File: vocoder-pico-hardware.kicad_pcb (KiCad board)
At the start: 2 copper layers, 57 x 108 mm, 68 parts, among them J1 Conn_02x05_Odd_Even, J2 AudioJack2_SwitchT, J3 AudioJack2_SwitchT, Q1 BC547, Q2 BC547, Q3 BC547, Q4 BC547, SW1 SW_Push, SW2 SW_Push, U1 TL072, U2 LM7805_TO220, U3 PCM5100A, U4 SC39-11GWA, U5 SC39-11GWA, U6 SC39-11GWA, U7 SC39-11GWA, U8 MCP6002-xP

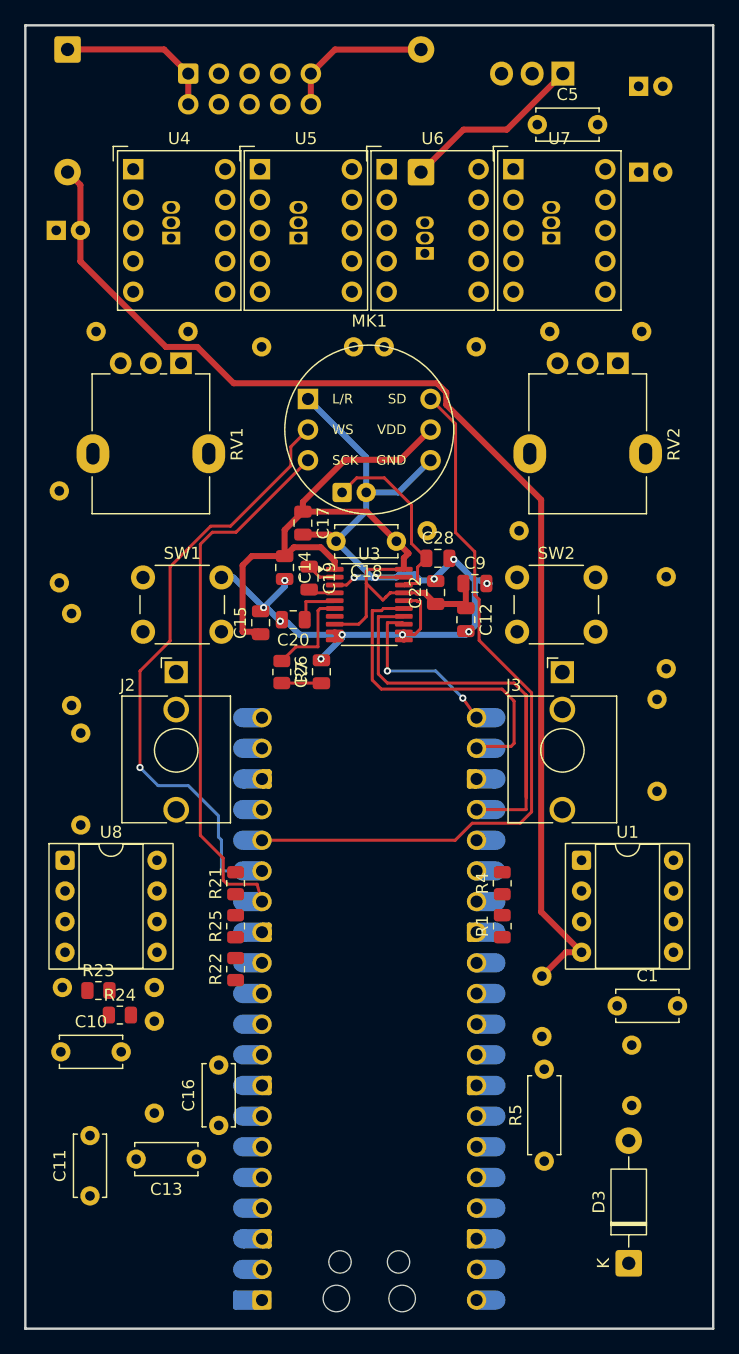
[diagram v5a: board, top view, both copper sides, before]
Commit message: improve power supply placement and routing
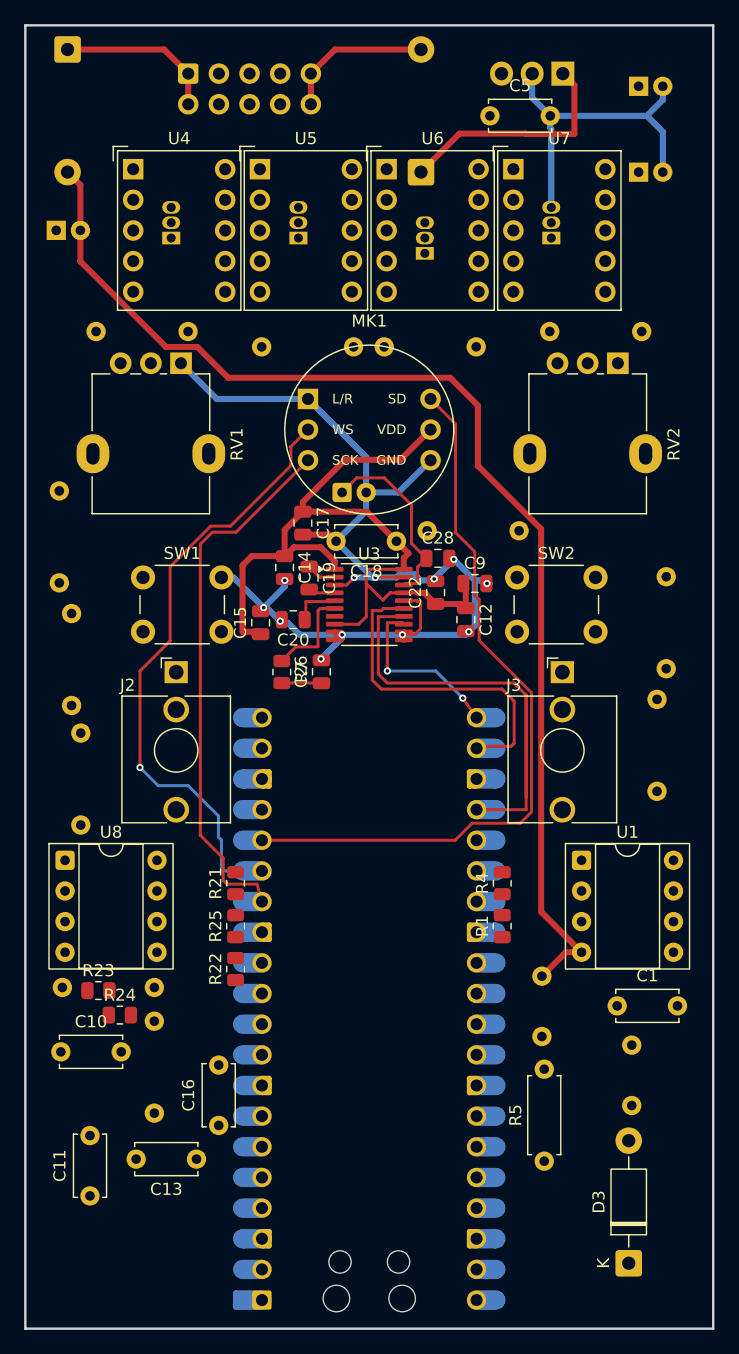
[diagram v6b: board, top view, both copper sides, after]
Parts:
- moved C5 3.99 mm to (87.5, 37.5)
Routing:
- net GND: track 86.9 -> 126.6 mm
- net +12V: track 15.1 -> 19.4 mm
- net -12V: track 97.8 -> 98.7 mm
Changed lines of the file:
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@@
 	(footprint "Capacitor_THT:C_Disc_D5.0mm_W2.5mm_P5.00mm"
 		(layer "F.Cu")
-		(at 91.4235 38.227)
+		(at 87.5 37.5)
 		(descr "C, Disc series, Radial, pin pitch=5.00mm, diameter*width=5*2.5mm^2, Capacitor, http://cdn-reichelt.de/documents/datenblatt/B300/DS_KERKO_TC.pdf")
 		(tags "C Disc series Radial pin pitch 5.00mm diameter 5mm width 2.5mm Capacitor")
@@
 	)
 	(segment
+		(start 101.822 36.18337)
+		(end 101.822 35.052)
+		(width 0.5)
+		(layer "B.Cu")
+		(net 1)
+	)
+	(segment
+		(start 72.42 60.96)
+		(end 64.86 60.96)
+		(width 0.5)
+		(layer "B.Cu")
+		(net 1)
+	)
+	(segment
 		(start 86.25 76)
 		(end 84.5 74.25)
@@
 	)
 	(segment
+		(start 100.50537 37.5)
+		(end 101.822 38.81663)
+		(width 0.5)
+		(layer "B.Cu")
+		(net 1)
+	)
+	(segment
 		(start 84.25 74)
 		(end 84.25 74.5)
@@
 	)
 	(segment
+		(start 91 36)
+		(end 91 34)
+		(width 0.5)
+		(layer "B.Cu")
+		(net 1)
+	)
+	(segment
 		(start 79.75 75.75)
 		(end 78 75.75)
@@
 	)
 	(segment
+		(start 92.5 37.5)
+		(end 91 36)
+		(width 0.5)
+		(layer "B.Cu")
+		(net 1)
+	)
+	(segment
 		(start 81.25 75.5)
 		(end 80 75.5)
@@
 	)
 	(segment
+		(start 92.583 38.583)
+		(end 92.583 45.085)
+		(width 0.5)
+		(layer "B.Cu")
+		(net 1)
+	)
+	(segment
 		(start 77.75 75.75)
 		(end 74.75 72.75)
@@
 	)
 	(segment
+		(start 92.5 37.5)
+		(end 92.5 38.5)
+		(width 0.5)
+		(layer "B.Cu")
+		(net 1)
+	)
+	(segment
 		(start 85.5 80.5)
 		(end 85.75 80.25)
@@
 	)
 	(segment
+		(start 92.5 38.5)
+		(end 92.583 38.583)
+		(width 0.5)
+		(layer "B.Cu")
+		(net 1)
+	)
+	(segment
+		(start 64.86 60.96)
+		(end 61.9 58)
+		(width 0.5)
+		(layer "B.Cu")
+		(net 1)
+	)
+	(segment
+		(start 92.5 37.5)
+		(end 100.50537 37.5)
+		(width 0.5)
+		(layer "B.Cu")
+		(net 1)
+	)
+	(segment
 		(start 80.25 80.5)
 		(end 85.5 80.5)
@@
 	)
 	(segment
+		(start 100.50537 37.5)
+		(end 101.822 36.18337)
+		(width 0.5)
+		(layer "B.Cu")
+		(net 1)
+	)
+	(segment
 		(start 84.5 74.25)
 		(end 84.25 74)
@@
 	)
 	(segment
+		(start 101.822 38.81663)
+		(end 101.822 42.164)
+		(width 0.5)
+		(layer "B.Cu")
+		(net 1)
+	)
+	(segment
 		(start 87.25 76.25)
 		(end 87.5 76.25)
@@
 	)
 	(segment
-		(start 60.649 56.649)
-		(end 63.251 56.649)
+		(start 91.744308 71.744308)
+		(end 91.744308 103.464308)
 		(width 0.5)
 		(layer "F.Cu")
@@
 	)
 	(segment
-		(start 91.744308 69.30972)
-		(end 91.744308 103.464308)
+		(start 84.199 59.199)
+		(end 86.5 61.5)
 		(width 0.5)
 		(layer "F.Cu")
@@
 	)
 	(segment
-		(start 83.881 60.421108)
-		(end 83.881 61.446412)
+		(start 91.744308 103.464308)
+		(end 95.09 106.81)
 		(width 0.5)
 		(layer "F.Cu")
@@
 	)
 	(segment
-		(start 53.562 49.562)
-		(end 60.649 56.649)
+		(start 95.09 106.81)
+		(end 93.787 106.81)
 		(width 0.5)
 		(layer "F.Cu")
@@
 	)
 	(segment
-		(start 95.09 106.81)
-		(end 93.787 106.81)
+		(start 86.5 61.5)
+		(end 86.5 66.5)
 		(width 0.5)
 		(layer "F.Cu")
@@
 	)
 	(segment
-		(start 91.744308 103.464308)
-		(end 95.09 106.81)
+		(start 65.801 59.199)
+		(end 84.199 59.199)
 		(width 0.5)
 		(layer "F.Cu")
@@
 	)
 	(segment
-		(start 53.562 43.222)
-		(end 53.562 46.99)
+		(start 63.251 56.649)
+		(end 65.801 59.199)
 		(width 0.5)
 		(layer "F.Cu")
@@
 	)
 	(segment
-		(start 53.562 46.99)
-		(end 53.562 49.562)
+		(start 53.562 43.222)
+		(end 53.562 46.99)
 		(width 0.5)
 		(layer "F.Cu")
@@
 	)
 	(segment
-		(start 66.261 59.659)
-		(end 83.118892 59.659)
+		(start 86.5 66.5)
+		(end 91.744308 71.744308)
 		(width 0.5)
 		(layer "F.Cu")
@@
 	)
 	(segment
-		(start 83.881 61.446412)
-		(end 91.744308 69.30972)
+		(start 53.562 49.562)
+		(end 60.649 56.649)
 		(width 0.5)
 		(layer "F.Cu")
@@
 	)
 	(segment
-		(start 93.787 106.81)
-		(end 91.805 108.792)
+		(start 60.649 56.649)
+		(end 63.251 56.649)
 		(width 0.5)
 		(layer "F.Cu")
@@
 	)
 	(segment
-		(start 63.251 56.649)
-		(end 66.261 59.659)
+		(start 53.562 46.99)
+		(end 53.562 49.562)
 		(width 0.5)
 		(layer "F.Cu")
@@
 	)
 	(segment
-		(start 83.118892 59.659)
-		(end 83.881 60.421108)
+		(start 93.787 106.81)
+		(end 91.805 108.792)
 		(width 0.5)
 		(layer "F.Cu")
@@
 	)
 	(segment
+		(start 90.476 38.976)
+		(end 90.5 39)
+		(width 0.5)
+		(layer "F.Cu")
+		(net 36)
+	)
+	(segment
 		(start 81.788 42.164)
-		(end 85.312349 38.639651)
+		(end 84.976 38.976)
 		(width 0.5)
 		(layer "F.Cu")
@@
 	)
 	(segment
-		(start 88.900349 38.639651)
+		(start 90.5 39)
+		(end 94.5 39)
+		(width 0.5)
+		(layer "F.Cu")
+		(net 36)
+	)
+	(segment
+		(start 94.5 34.96)
 		(end 93.54 34)
 		(width 0.5)
@@
 	)
 	(segment
-		(start 85.312349 38.639651)
-		(end 88.900349 38.639651)
+		(start 84.976 38.976)
+		(end 90.476 38.976)
+		(width 0.5)
+		(layer "F.Cu")
+		(net 36)
+	)
+	(segment
+		(start 94.5 39)
+		(end 94.5 34.96)
 		(width 0.5)
 		(layer "F.Cu")

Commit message: finalize power supply placement and routing
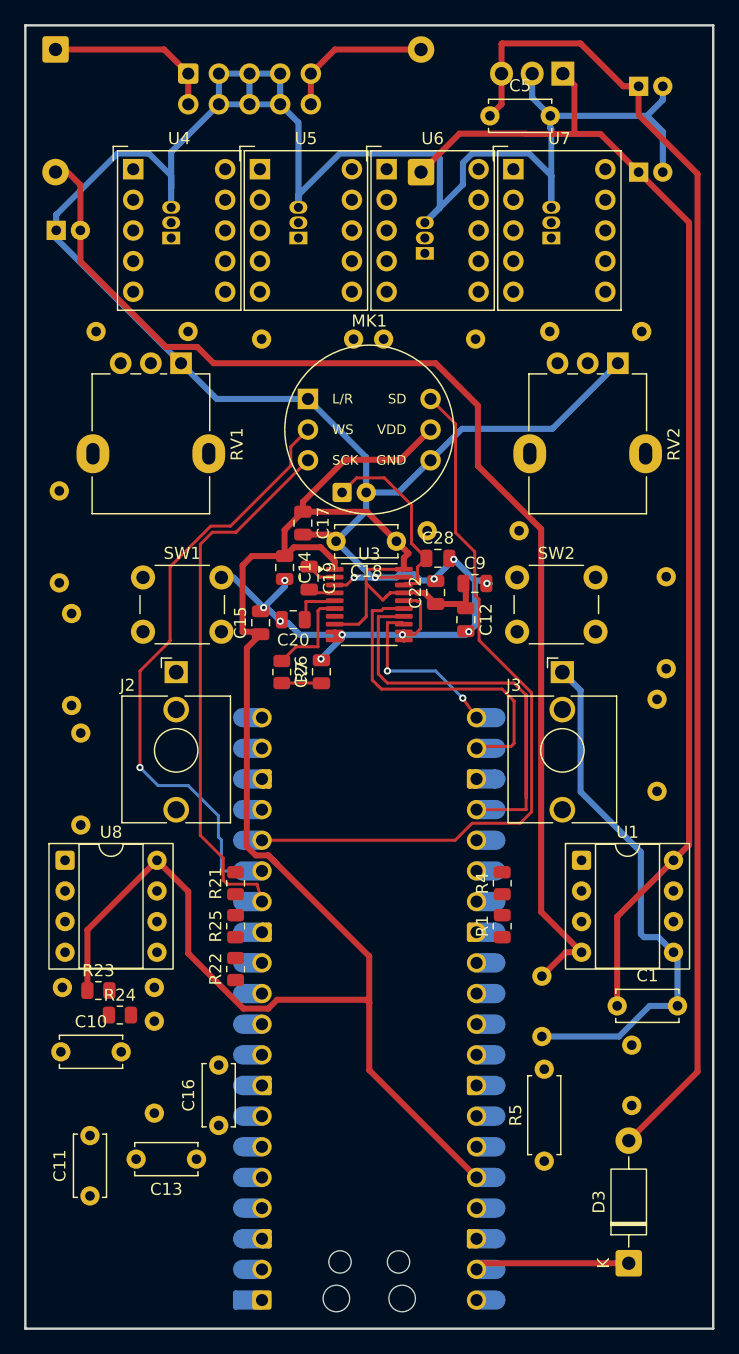
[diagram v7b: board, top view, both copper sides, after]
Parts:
- moved D2 1.00 mm to (51.5, 32.0)
- moved R19 0.64 mm to (78.7, 56.0)
- moved R18 0.64 mm to (68.6, 56.0)
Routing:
- net GND: track 126.6 -> 294.7 mm
- net +5V: track 0.00 -> 111.8 mm
- net Vdd: track 68.9 -> 163.3 mm
- net +12V: track 19.4 -> 99.4 mm
- net Vsys: track 0.00 -> 12.8 mm

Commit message: replacing jacks to the bottom of the pcb
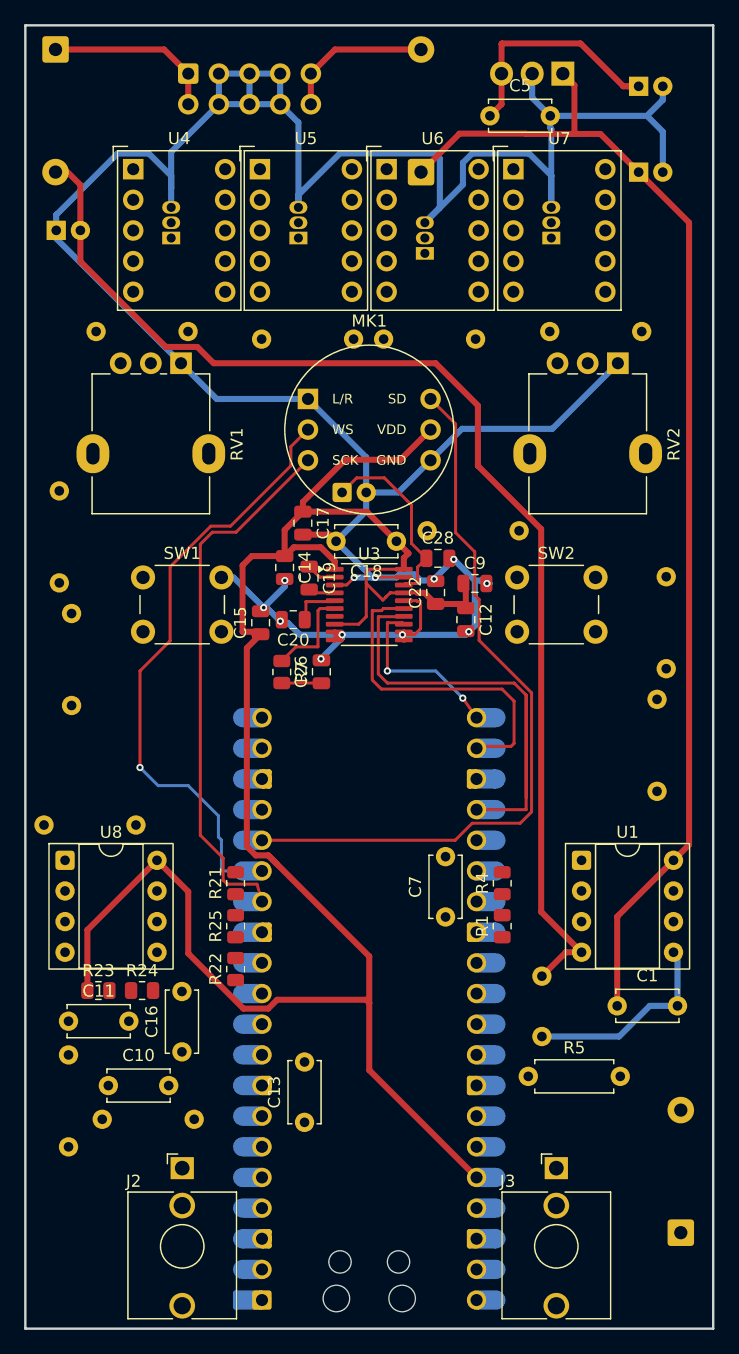
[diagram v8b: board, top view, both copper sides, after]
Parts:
- C7: moved to F.Cu
- D3: moved to B.Cu
- moved J2 41.1 mm to (62.0, 124.7)
- moved J3 41.1 mm to (93.0, 124.7)
- moved C7 22.0 mm to (83.8, 103.9)
- moved C11 14.6 mm to (52.6, 112.5), turned to 0 degrees
- moved R14 13.2 mm to (52.6, 122.9), turned to 90 degrees
- moved C13 9.46 mm to (72.1, 120.9), turned to 90 degrees
- moved R5 7.15 mm to (90.7, 117.1), turned to 0 degrees
- moved C16 6.82 mm to (62.0, 115.1)
- moved D3 5.00 mm to (103.3, 130.0)
- moved C10 4.83 mm to (55.9, 117.9)
- moved R16 4.35 mm to (55.4, 120.7), turned to 0 degrees
- moved R13 3.05 mm to (50.5, 96.3), turned to 0 degrees
- moved R24 2.74 mm to (58.7, 110.0)
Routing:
- net +5V: track 111.8 -> 20.1 mm
- net GND: track 294.7 -> 267.0 mm
- net Vsys: track 12.8 -> 0.00 mm
